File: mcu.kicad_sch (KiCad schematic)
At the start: 1 part, among them U1 STM32G071C8Tx

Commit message: Wire more stuff
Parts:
- added C21: 4.7uF, symbol Device:C
- added C22, C24: 100nF, symbol Device:C
- added C23: 1uF, symbol Device:C
- added C29, C30: 10pF, symbol Device:C
- added L2: 600R@100MHz, symbol Device:L
- added R22, R4: 4.7k, symbol Device:R
- added R23, R24: 100R, symbol Device:R
- added Y1: NX3225GD, Crystal:Crystal_SMD_3225-4Pin_3.2x2.5mm, symbol Device:Crystal_Small
- U1: JLCPCB Part No (none) -> C529341; LCSC Part No C529341 -> (none)
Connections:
- net ~{RESET}: now reaches U1.10 (PF2)
- net LED_PORT0.R: now reaches U1.12 (PA1)
- net LED_PORT0.G: now reaches U1.13 (PA2)
- net LED_PORT0.B: now reaches U1.14 (PA3)
- net I2C.SCL: now reaches U1.25 (PB13)
- net I2C.SCL: now also R4.2
- net I2C.SDA: now reaches U1.26 (PB14)
- net I2C.SDA: now also R22.2
- net UCDP1.CC2: now reaches U1.27 (PB15)
- net UCPD1.CC1: now reaches U1.28 (PA8)
- net GND: now reaches U1.29 (PA9/UCPD1_DBCC1)
- net GND: now also U1.32 (PA10/UCPD1_DBCC2), U1.7 (VSS), C21.2, C22.2, C23.2, C24.2, C29.1, C30.1, L2.2
- net SWD.SWDCLK: now reaches U1.35 (PA13)
- net SWD.SWDIO: now reaches U1.36 (PA14)
- net +3V3: now reaches U1.4 (VBAT)
- net +3V3: now also U1.5 (VREF+), U1.6 (VDD), C23.1, R22.1, R4.1
- net at U1.8 (PF0): now also R23.2
- net at U1.9 (PF1): now also R24.2
- new net: C21.1, C22.1, C24.1, L2.1
- new net: C30.2, R24.1, Y1.1
- new net: C29.2, R23.1, Y1.2
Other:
- note added: "- Hackady on USB PD: https://hackaday.com/2023/02/14/all-about-usb-c-talking-low-level-pd/"
- note added: "- ST32G0 UDPD: https://www.st.com/resource/en/product_training/STM32G0-Peripheral-USB-Type-C-Power-Delivery-UCPD.pdf"
- note added: "- USB PD primer (TI): https://www.ti.com/lit/wp/slyy109b/slyy109b.pdf?ts=1711082549009"
- note added: "Are these the correct DBCC pins to connect to ground?"
- note added: "TODO: verify pullup resistance value"

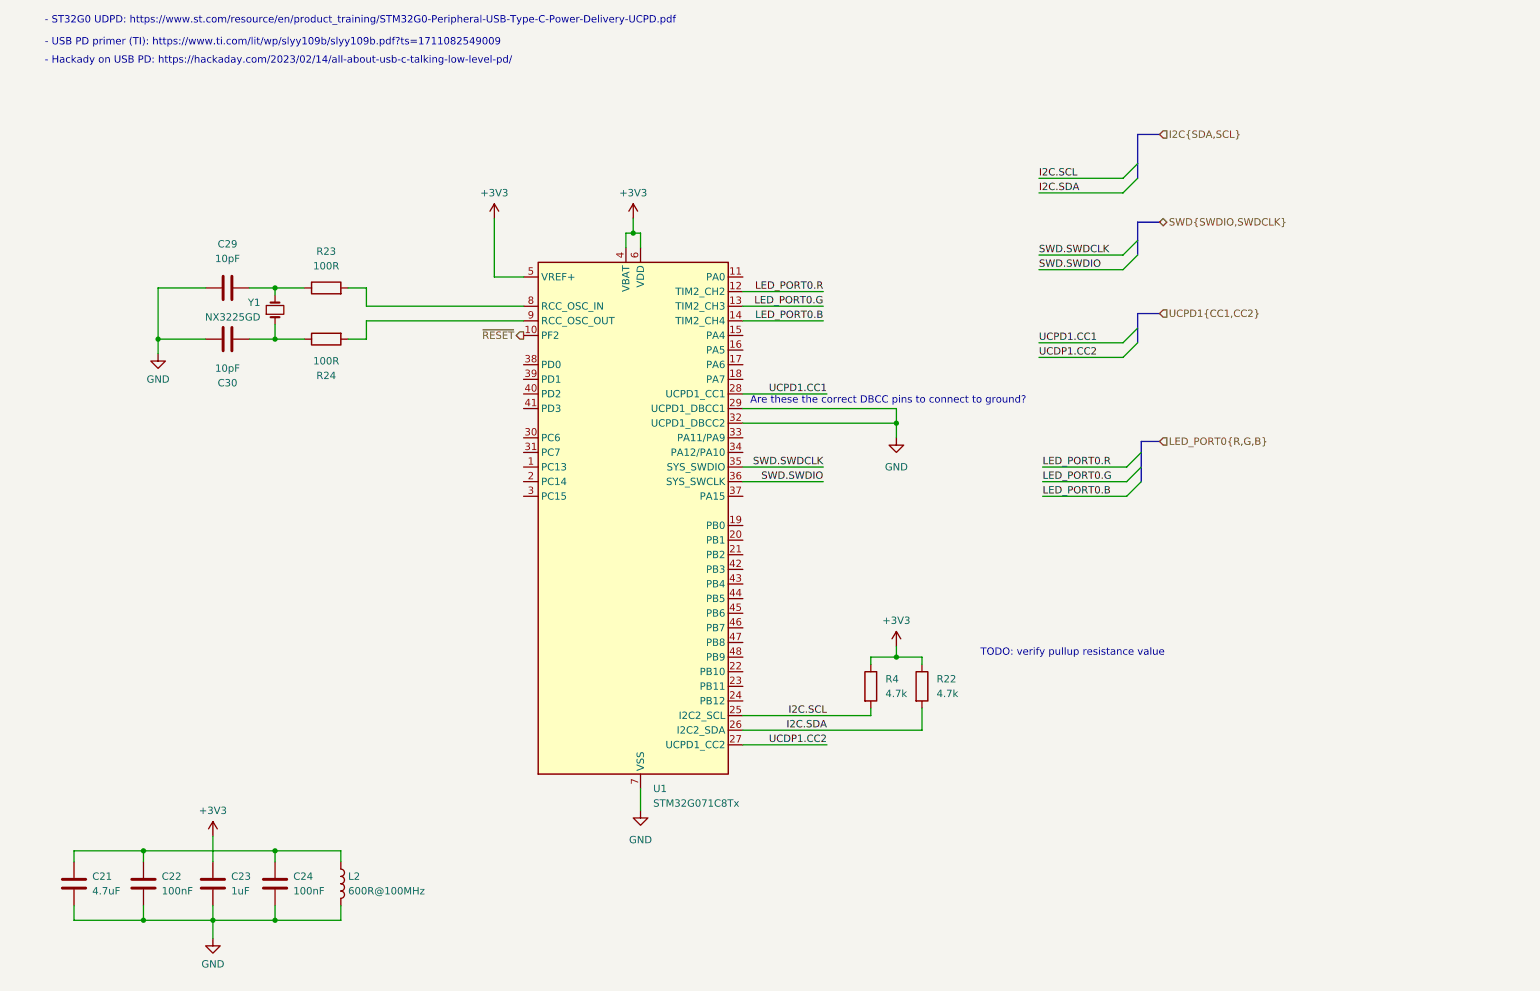
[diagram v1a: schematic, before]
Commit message: Add test points, notes on VCONN
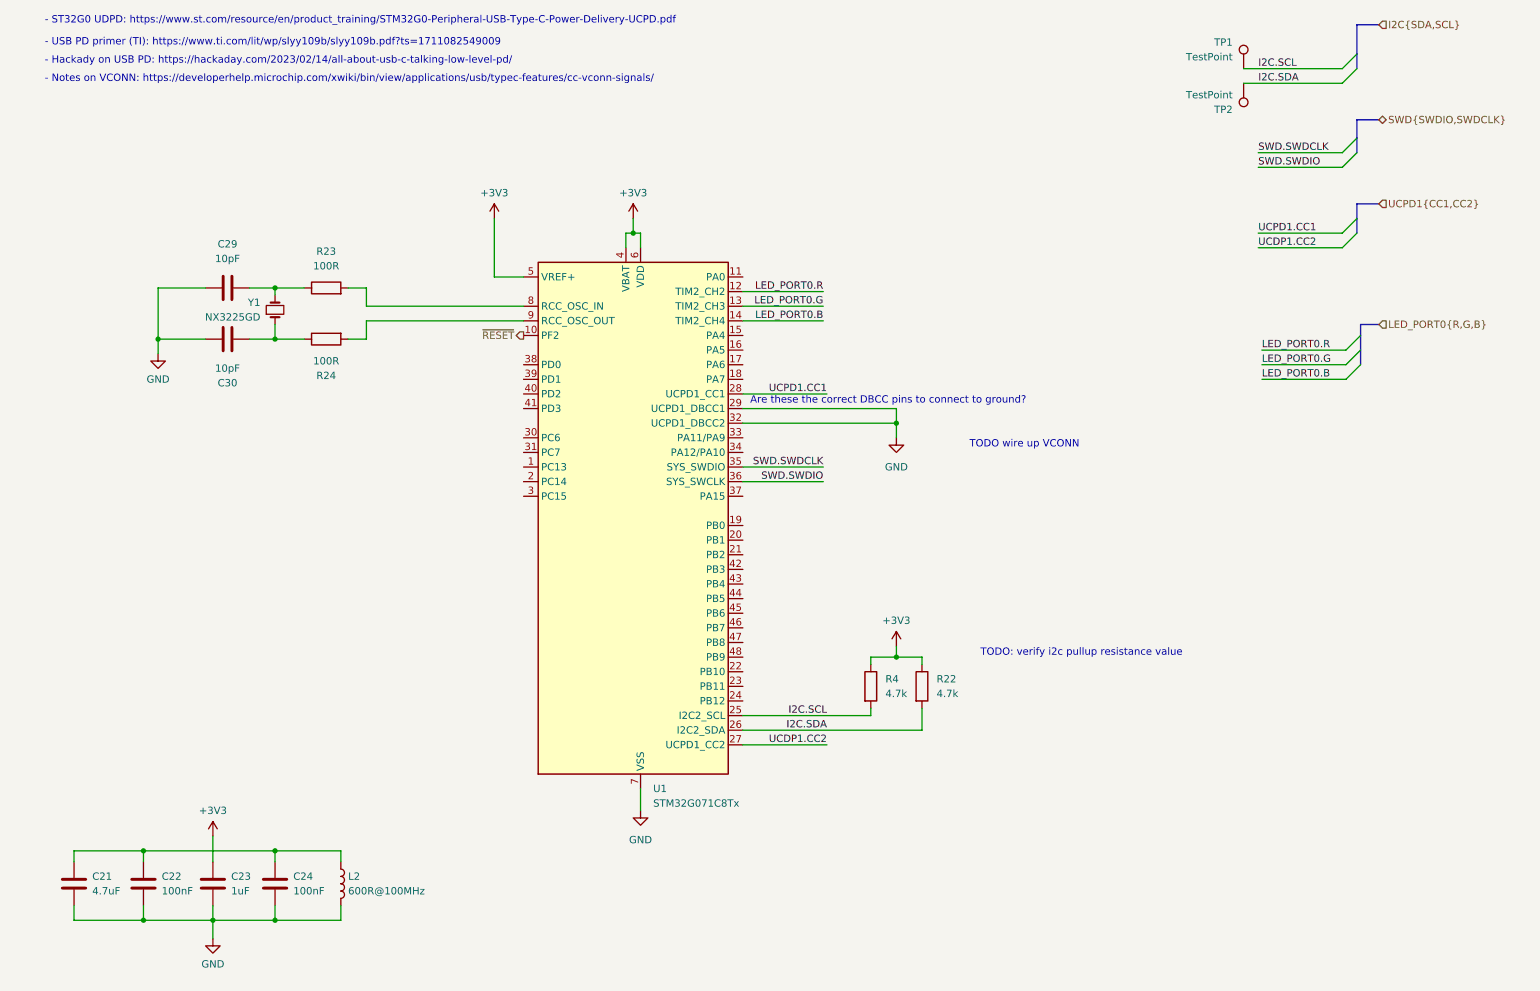
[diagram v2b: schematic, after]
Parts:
- added TP1, TP2: TestPoint, symbol Connector:TestPoint
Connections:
- net I2C.SCL: now also TP1.1
- net I2C.SDA: now also TP2.1
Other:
- note added: "- Notes on VCONN: https://developerhelp.microchip.com/xwiki/bin/view/applications/usb/typec-features/cc-vconn-signals/"
- note added: "TODO wire up VCONN"
- note added: "TODO: verify i2c pullup resistance value"
- note removed: "TODO: verify pullup resistance value"

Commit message: Whole bunch of changes to all kinds of things
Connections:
- net NCP0_EN: now reaches U1.30 (PC6)
- net NCP0_INT: now reaches U1.31 (PC7)
- net NCP0_CLIND: now reaches U1.33 (PA11/PA9)
- net LED_PORT0.B: no longer names the net of U1.14 (PA3)
- net UCDP1.CC2 renamed UCPD1.CC2
- no-connect marks 0 -> 28
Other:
- note added: "TODO wire up VCONN using TCPP02-M18 (X-NUCLEO-SRC1M1)"
- note removed: "Are these the correct DBCC pins to connect to ground?"
- note removed: "TODO wire up VCONN"
- moved on the sheet: C22, C24, C29, C30, L2, R23, R24, TP1, TP2, U1, Y1

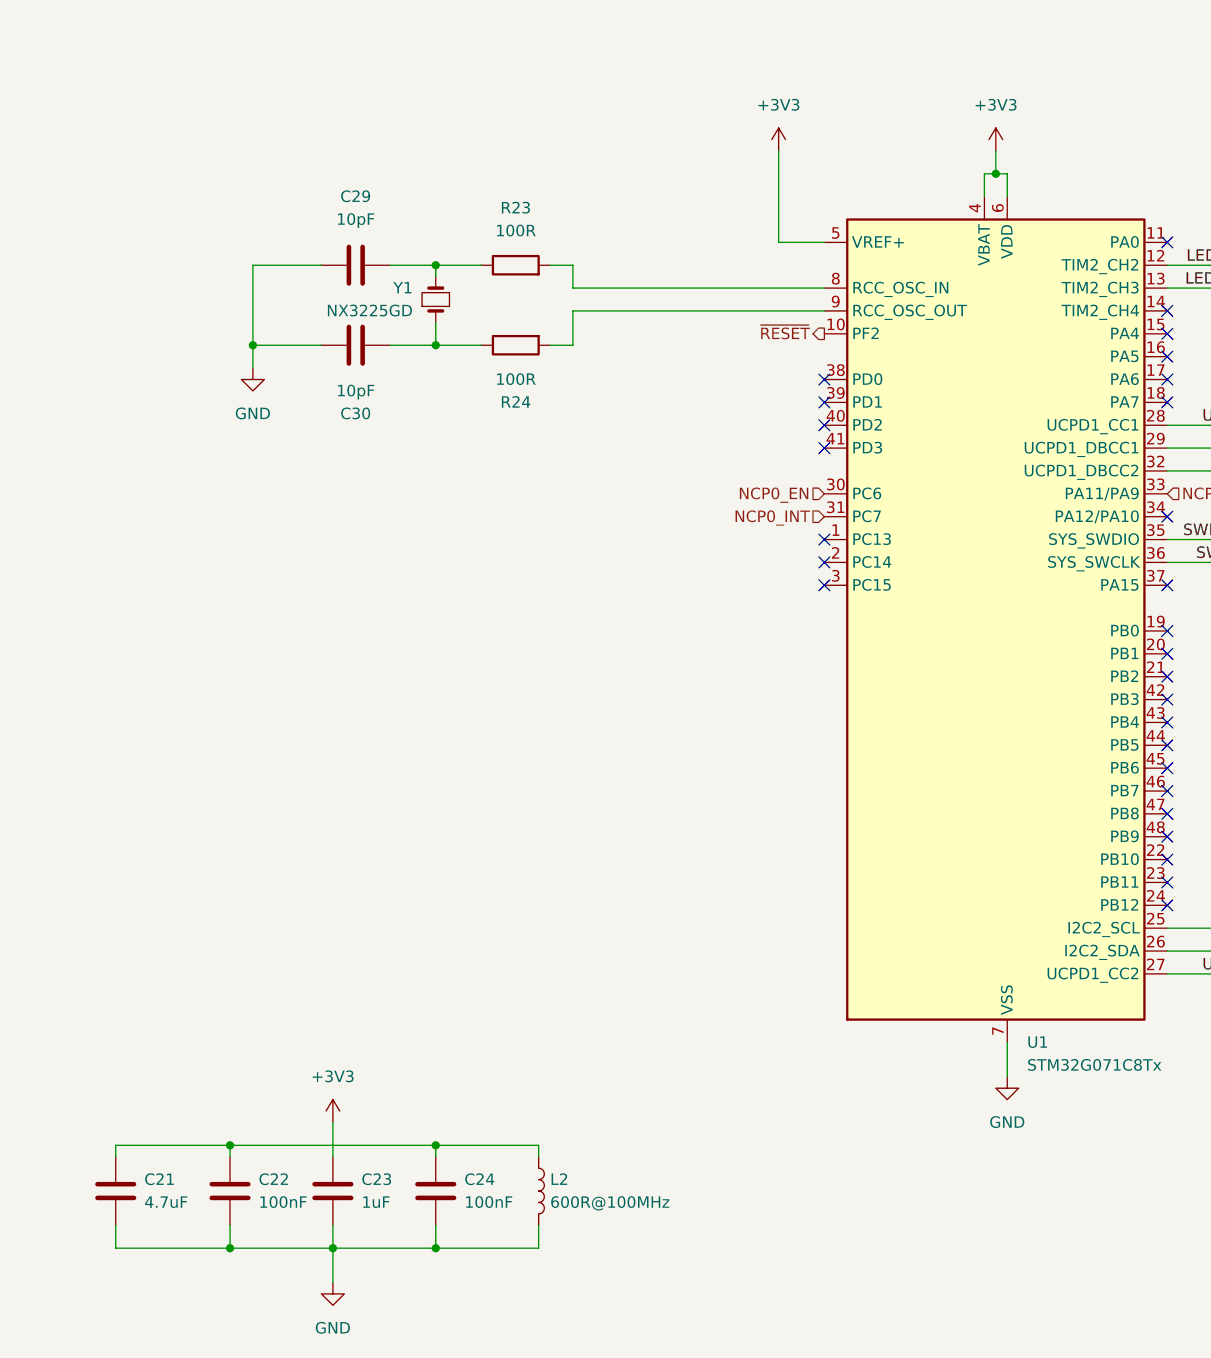
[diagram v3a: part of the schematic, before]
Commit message: Review Switcher and part of MCU
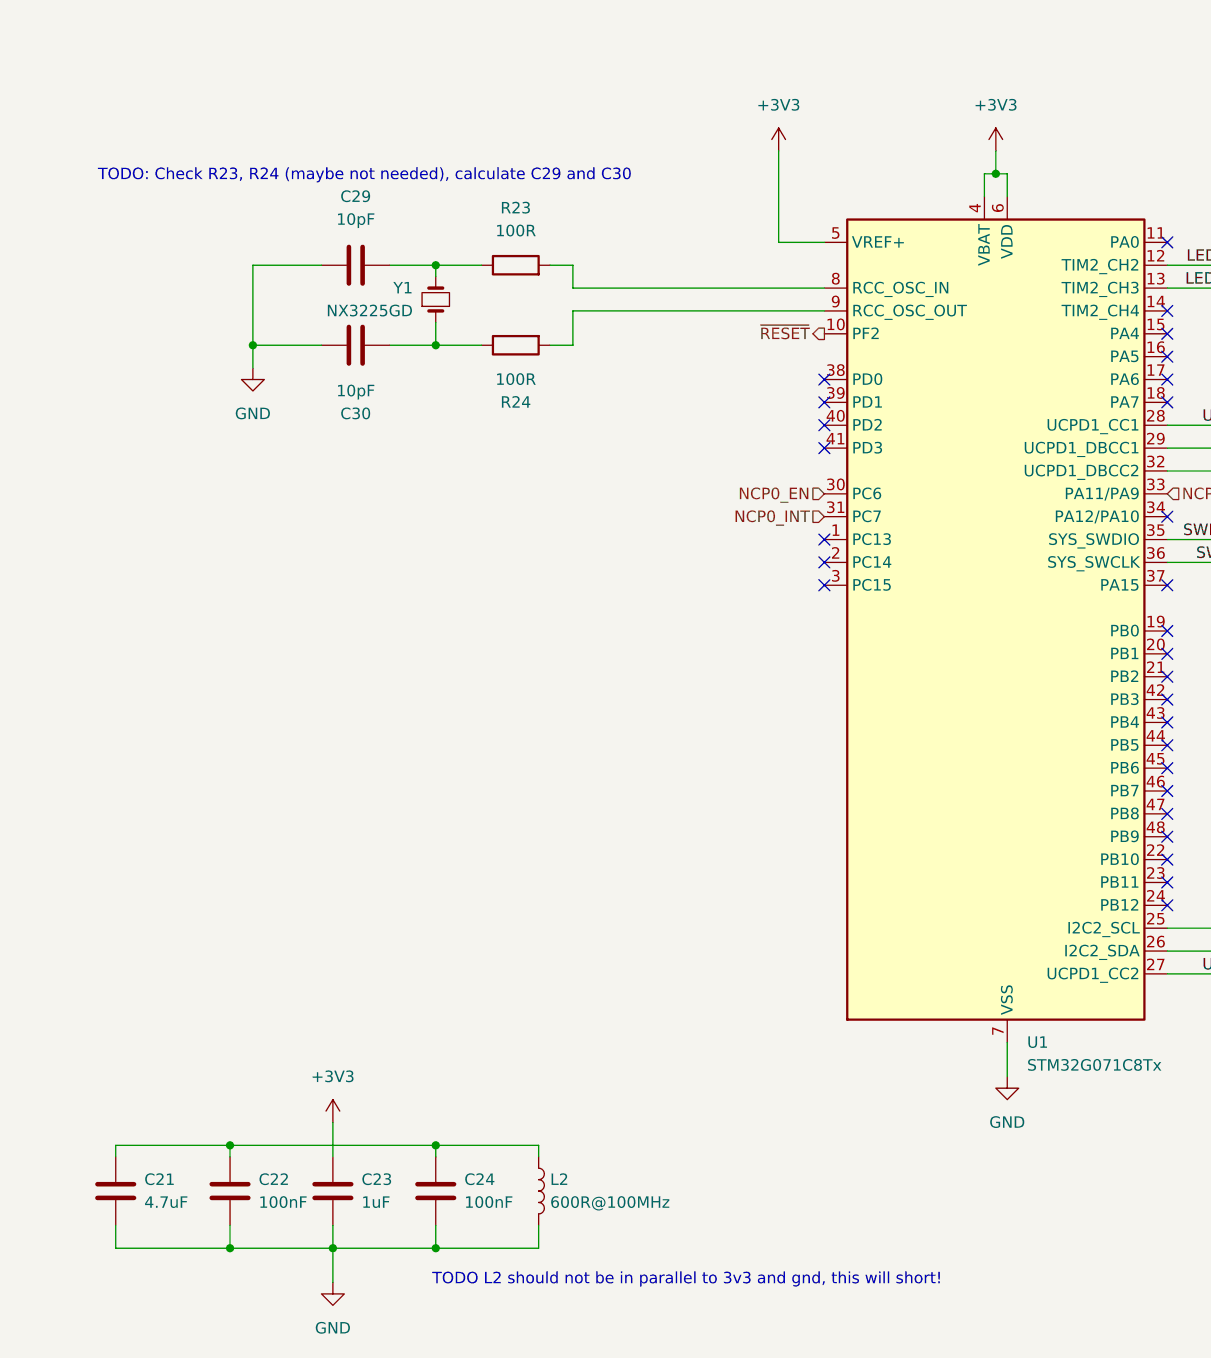
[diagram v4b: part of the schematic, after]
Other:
- note added: "TODO L2 should not be in parallel to 3v3 and gnd, this will short!"
- note added: "TODO: Check R23, R24 (maybe not needed), calculate C29 and C30"
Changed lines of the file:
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@@
+		)
+	)
+	(text "TODO L2 should not be in parallel to 3v3 and gnd, this will short!"
+		(exclude_from_sim no)
+		(at 96.52 182.626 0)
+		(effects
+			(font
+				(size 1.27 1.27)
+			)
 		)
 	)
@@
 		)
 	)
+	(text "TODO: Check R23, R24 (maybe not needed), calculate C29 and C30\n"
+		(exclude_from_sim no)
+		(at 60.706 59.944 0)
+		(effects
+			(font
+				(size 1.27 1.27)
+			)
+		)
+	)

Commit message: WIP on vconn
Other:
- note removed: "- Notes on VCONN: https://developerhelp.microchip.com/xwiki/bin/view/applications/usb/typec-features/cc-vconn-signals/"
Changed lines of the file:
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@@
-		)
-	)
-	(text "- Notes on VCONN: https://developerhelp.microchip.com/xwiki/bin/view/applications/usb/typec-features/cc-vconn-signals/"
-		(exclude_from_sim no)
-		(at 27.94 34.29 0)
-		(effects
-			(font
-				(size 1.27 1.27)
-			)
-			(justify left bottom)
-			(href "https://developerhelp.microchip.com/xwiki/bin/view/applications/usb/typec-features/cc-vconn-signals/")
 		)
 	)

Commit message: WIP on vconn
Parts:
- removed L2: 600R@100MHz, symbol Device:L
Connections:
- net +3V3: now also C21.1, C22.1, C24.1
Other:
- note removed: "TODO L2 should not be in parallel to 3v3 and gnd, this will short!"
- note removed: "TODO wire up VCONN using TCPP02-M18 (X-NUCLEO-SRC1M1)"
- moved on the sheet: C23, C24

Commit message: wire up vconn stuff
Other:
- note added: "TODO add VCONN_EN and VCONN_IANA"
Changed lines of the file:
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@@
+		)
+	)
+	(text "TODO add VCONN_EN and VCONN_IANA"
+		(exclude_from_sim no)
+		(at 209.042 113.792 0)
+		(effects
+			(font
+				(size 1.27 1.27)
+			)
 		)
 	)
@@
 		)
 	)
+	(hierarchical_label "VCONN_EN"
+		(shape output)
+		(at 237.49 99.06 0)
+		(fields_autoplaced yes)
+		(effects
+			(font
+				(size 1.27 1.27)
+			)
+			(justify left)
+		)
+	)
 	(hierarchical_label "NCP0_CLIND"
 		(shape input)
@@
 		)
 	)
+	(hierarchical_label "VCONN_IANA"
+		(shape input)
+		(at 237.49 105.41 0)
+		(fields_autoplaced yes)
+		(effects
+			(font
+				(size 1.27 1.27)
+			)
+			(justify left)
+		)
+	)
